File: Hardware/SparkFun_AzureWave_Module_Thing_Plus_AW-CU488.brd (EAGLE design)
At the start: 22.9 x 77.5 mm, 128 parts, among them J1 THING_PLUS, J2 LiPo, J3 QWIIC_RA, J5 USB-C, Q1 3.1A/30V/105mΩ, Q2 MBT3904DW1T1, U1 AW-CU488, U2 CP210X, U3 XC6222B331MR-G, U4 MCP73831

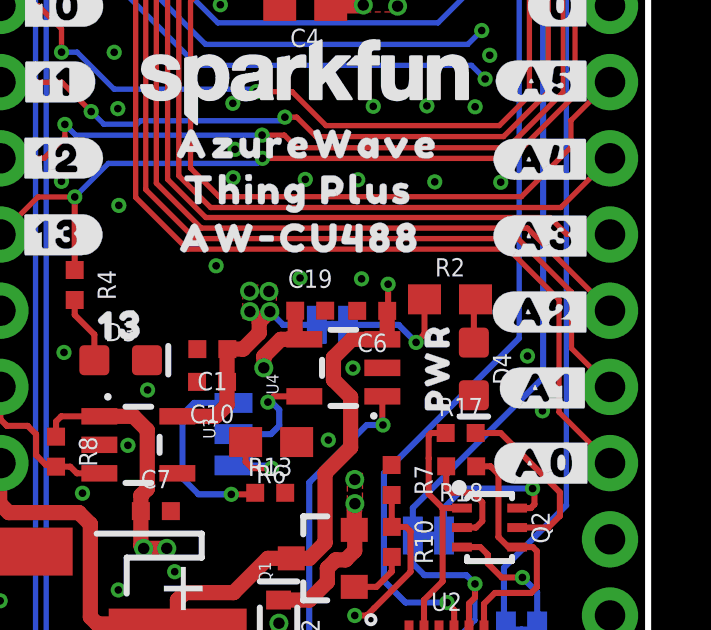
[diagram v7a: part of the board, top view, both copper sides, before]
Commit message: RED power LED limiting resistor reduced to 1K for better brightness matching
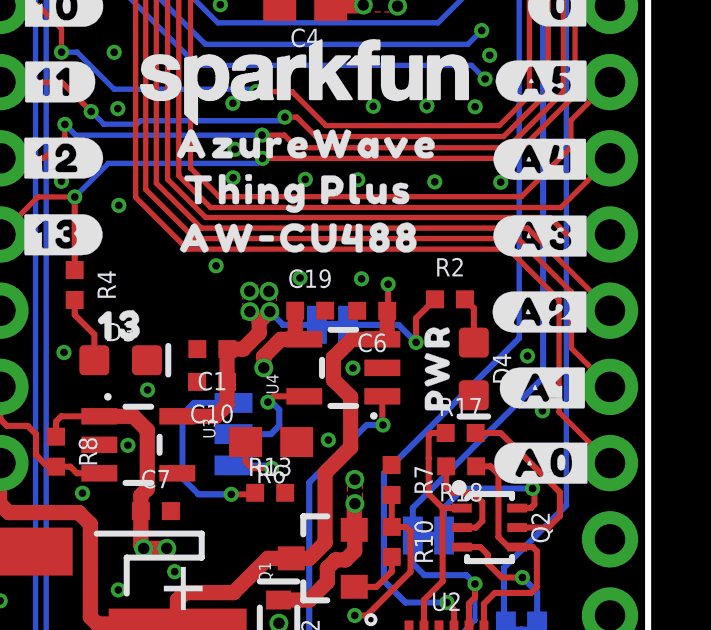
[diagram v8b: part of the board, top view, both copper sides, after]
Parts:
- R2: value 4.7k -> 1k; device SparkFun-Resistors:0603 -> SparkFun-Resistors:0402-TIGHT
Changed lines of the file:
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@@
 </element>
 <element name="U$20" library="output" package="#USBSHLD#GND#3" value="" x="12.573" y="3.429" smashed="yes" rot="MR0"/>
-<element name="R2" library="SparkFun-Resistors" package="0603" value="4.7k" x="16.256" y="29.5884625" smashed="yes">
+<element name="R2" library="SparkFun-Resistors" package="0402-TIGHT" value="1k" x="16.256" y="29.5884625" smashed="yes">
 <attribute name="NAME" x="16.256" y="30.3504625" size="0.6096" layer="25" font="vector" ratio="20" align="bottom-center"/>
-<attribute name="PROD_ID" value="RES-07857" x="16.256" y="29.5884625" size="1.778" layer="27" font="vector" ratio="15" display="off"/>
-<attribute name="VALUE" x="16.256" y="28.8264625" size="0.6096" layer="27" font="vector" ratio="20" align="top-center"/>
+<attribute name="PROD_ID" value="RES-14342" x="16.256" y="29.5884625" size="1.778" layer="27" font="vector" ratio="15" display="off"/>
+<attribute name="VALUE" value="1k" x="16.256" y="28.8264625" size="0.6096" layer="27" font="vector" ratio="20" align="top-center"/>
 </element>
 <element name="LED" library="SparkFun-Jumpers" package="SMT-JUMPER_2_NC_TRACE_SILK" package3d_urn="urn:adsk.eagle:package:39281/1" value="" x="12.336778125" y="28.7375625" smashed="yes" rot="MR180">
@@
 <contactref element="R2" pad="1"/>
 <contactref element="LED" pad="2"/>
-<wire x1="15.406" y1="29.5884625" x2="15.406" y2="28.433659375" width="0.2032" layer="1"/>
-<wire x1="15.406" y1="28.433659375" x2="15.1257" y2="28.153359375" width="0.2032" layer="1"/>
 <via x="15.1257" y="28.153359375" extent="1-16" drill="0.254"/>
 <wire x1="12.857478125" y1="28.7375625" x2="14.541496875" y2="28.7375625" width="0.2032" layer="16"/>
 <wire x1="14.541496875" y1="28.7375625" x2="15.1257" y2="28.153359375" width="0.2032" layer="16"/>
+<wire x1="15.1257" y1="28.153359375" x2="15.1257" y2="28.9581625" width="0.2032" layer="1"/>
+<wire x1="15.1257" y1="28.9581625" x2="15.756" y2="29.5884625" width="0.2032" layer="1"/>
 </signal>
 <signal name="N$14">
 <contactref element="R2" pad="2"/>
 <contactref element="D4" pad="A"/>
-<wire x1="17.106" y1="29.5884625" x2="17.05101875" y2="29.53348125" width="0.2032" layer="1"/>
-<wire x1="17.05101875" y1="29.53348125" x2="17.05101875" y2="28.146440625" width="0.2032" layer="1"/>
+<wire x1="17.05101875" y1="28.146440625" x2="17.05101875" y2="29.29344375" width="0.2032" layer="1"/>
+<wire x1="17.05101875" y1="29.29344375" x2="16.756" y2="29.5884625" width="0.2032" layer="1"/>
 </signal>
 <signal name="N$15">
